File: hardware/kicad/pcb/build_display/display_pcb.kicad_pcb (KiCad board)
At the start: 2 copper layers, 85 x 65 mm, 43 parts, among them J1 Wurth_615008145521, J2 JST_S8B-PH-K-S, J3 ESP-Prog, J5 TERM, U1 R-78E3.3-0.5, U2 THVD1400DR, U3-LDO AP2112K-3.3, U4-MUX TPS2116DRLR

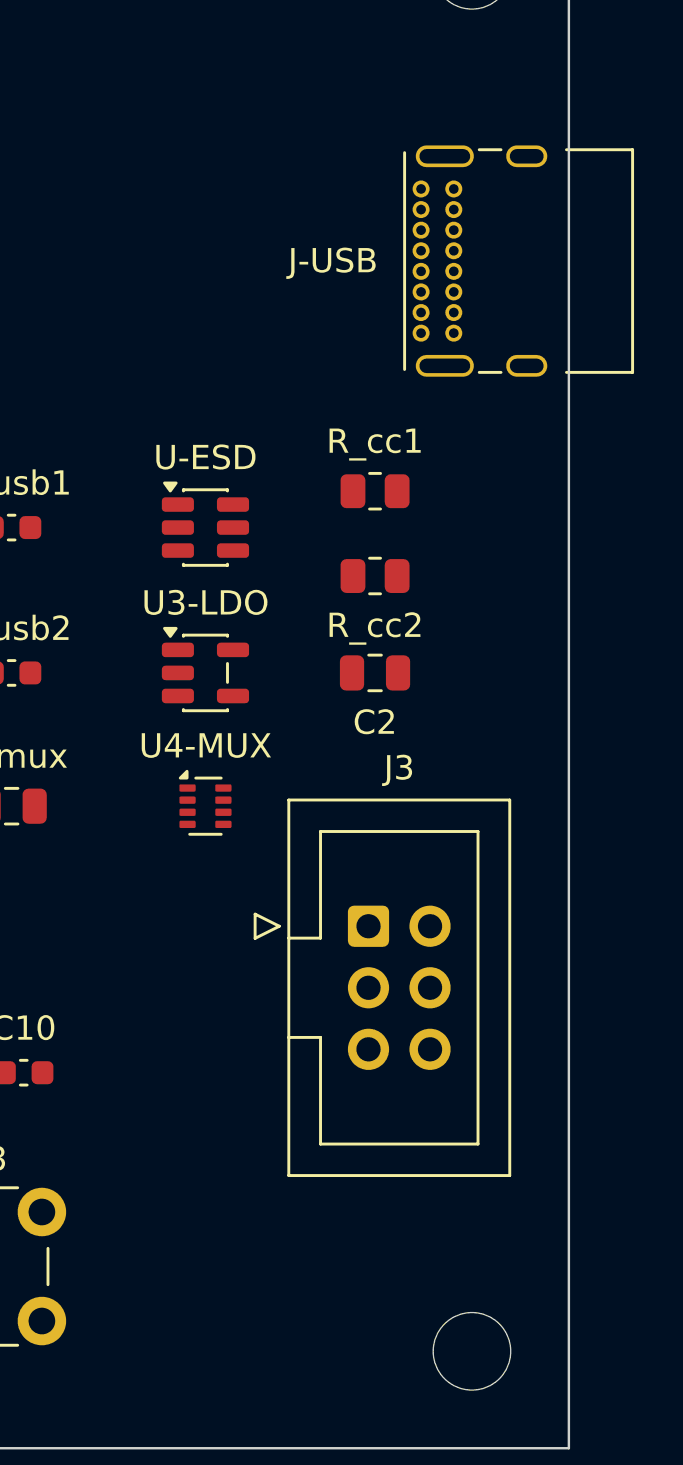
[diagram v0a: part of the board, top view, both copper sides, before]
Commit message: cp4: D40 vertical USB-C (resolves DR-35) + D41 no signing keys (resolves DR-34)
D40 - the edge-mount USB4085 could not be plugged inside the wall box (~5mm
past any board edge vs a plug needing 15-20mm; popping the faceplate exposes
the board FRONT, not its edges). User chose the vertical option: it opens +Z
and is reachable straight-on once the faceplate and e-paper module come away,
and is invisible when assembled.

Part is GCT USB4115-03-C (9.30mm) rather than the shorter USB4120 (6.5mm),
deliberately trading depth for footprint provenance: KiCad ships a footprint
for the 4115 citing GCT's official drawing and none for the 4120, and
hand-authoring a 0.5mm-pitch connector land pattern is the exact risk class
that produced DR-33 and the CP3 mating-face defect. Depth is affordable here;
a wrong land pattern is not.

Checked rather than assumed: pin table cross-read against the drawing (the
footprint's A1-A12/B1-B12/SH pads are a superset of our 16-pin symbol, so
every pin binds and the 8 SuperSpeed pads float); 30/30 pad tuples identical
to the library so the lib_footprint_mismatch is the same serialisation class
(evidence in iter1/jusb_pad_diff.txt); nothing overhangs a board edge any
more, so the E-edge whitelist is gone and silk_edge_clearance went 2 -> 0.
I ALSO CORRECTED MYSELF: I had claimed the taller part would force a longer
button plunger. It does not - with the 15mm plunger already locked the
protrusion is 2.3mm, inside the 2-3mm spec. The arithmetic is in D40.

Depth stack re-driven: J-USB 9.30mm displaces J3's 9.1mm, so gap ~9.7mm and
stack ~34.7mm against ~45mm usable. Battery board KEEPS USB4085 - it is not
in a wall box and its edge mount is correct there.

D41 - RPA sign-off stays name-based (git authorship), no signing keys. The
limit is stated in the gate's docstring rather than papered over, and the
threat model in REVIEWER_PATCH_POLICY.md explains why it is proportionate.

Stale-claim sweep after the change: requirements.md's exact-part list sti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
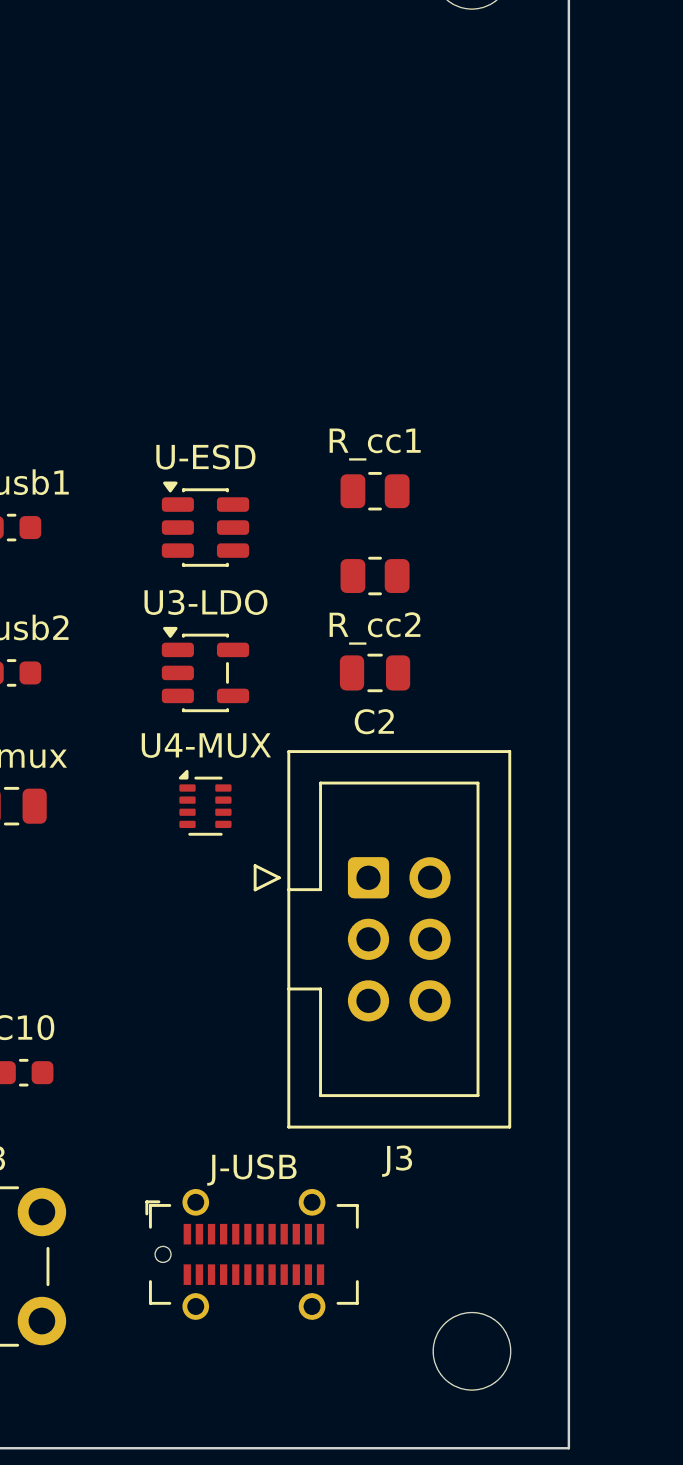
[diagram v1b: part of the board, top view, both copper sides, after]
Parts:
- removed the J-USB at (78.9, 19.0)
- added J-USB: USB4115-03-C, Connector_USB:USB_C_Receptacle_GCT_USB4115-03-C, F.Cu at (72.0, 57.0)
- moved J3 2.00 mm to (76.7, 41.5)

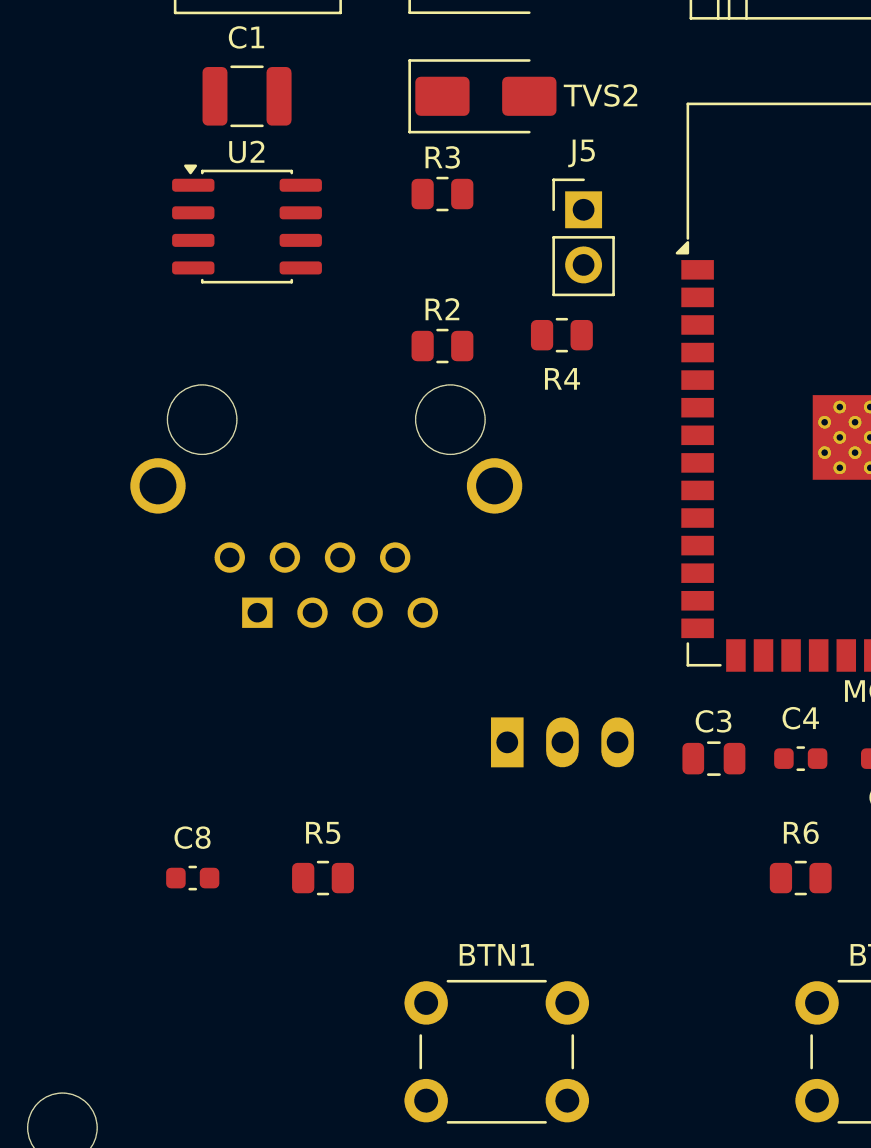
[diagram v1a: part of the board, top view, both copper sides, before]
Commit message: cp4 iter2: F01 back-side centre transform (4th site) + F02 wrong-order SKUs
F01 BLOCKER, confirmed and fixed at root. cc() in BOTH pcb builds still
negated local X while the writer and gates negate Y - the FOURTH site of a
transform I had "swept" twice. Reproduced the reviewer's numbers exactly: J1
requested (9.8,46.5) actually landed at (16.15,28.06), U1 (22,41) at
(26.97,45.50). The fix is not an axis edit: cc() now delegates to core._xf so
the project has exactly ONE back-side transform. A duplicated transform was
the bug; sharing it is the fix.

The J1 orientation assert was tautological, as reported - it compared two
symmetric X centroids, equal by construction. Replaced with a real probe: the
signal pads sit at one end of the footprint and the body extends away from
them, so the pads->courtyard-centre vector IS the opening direction. J1 is
now rot 90 on the back and that vector reads (-7.95,+0.00) = due west.

Re-placed for the three conflicts the corrected transform exposed (BTN1 into
J1 pads, J1 pads into R5, J1 courtyard into U1): J1 to (11,30), U1 to
(12,48), U2 to (25.5,33.5), R2 to (27,29). All gates and DRC clean; parts now
land exactly at their requested centres (error 0.00).

F02 IMPORTANT, confirmed by live POST /resolve: 455-1710-ND -> B8B-PH-K-S
(the REJECTED top-entry part) and 640-USB4085-GF-A -> USB4085-GF-A (the
retired edge part). Both cells would have ordered the wrong physical object.
Cause was incomplete propagation twice over - D39 changed the MPN text but
never re-resolved the order code, and D40 updated one distributor column and
not the other. Corrected both, plus the stale J-USB prose in
cp1_display_side.md and the J2 description that said "S8B" for both entries.

New persistent coverage: a ROW-SCOPED coherence check (a display BOM row must
not carry an order code that resolves to a different part than its own MPN).
Deliberately row-scoped, not a SUPERSEDED token, because the BATTERY J3
legitimately orders USB4085 through that exact Mo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
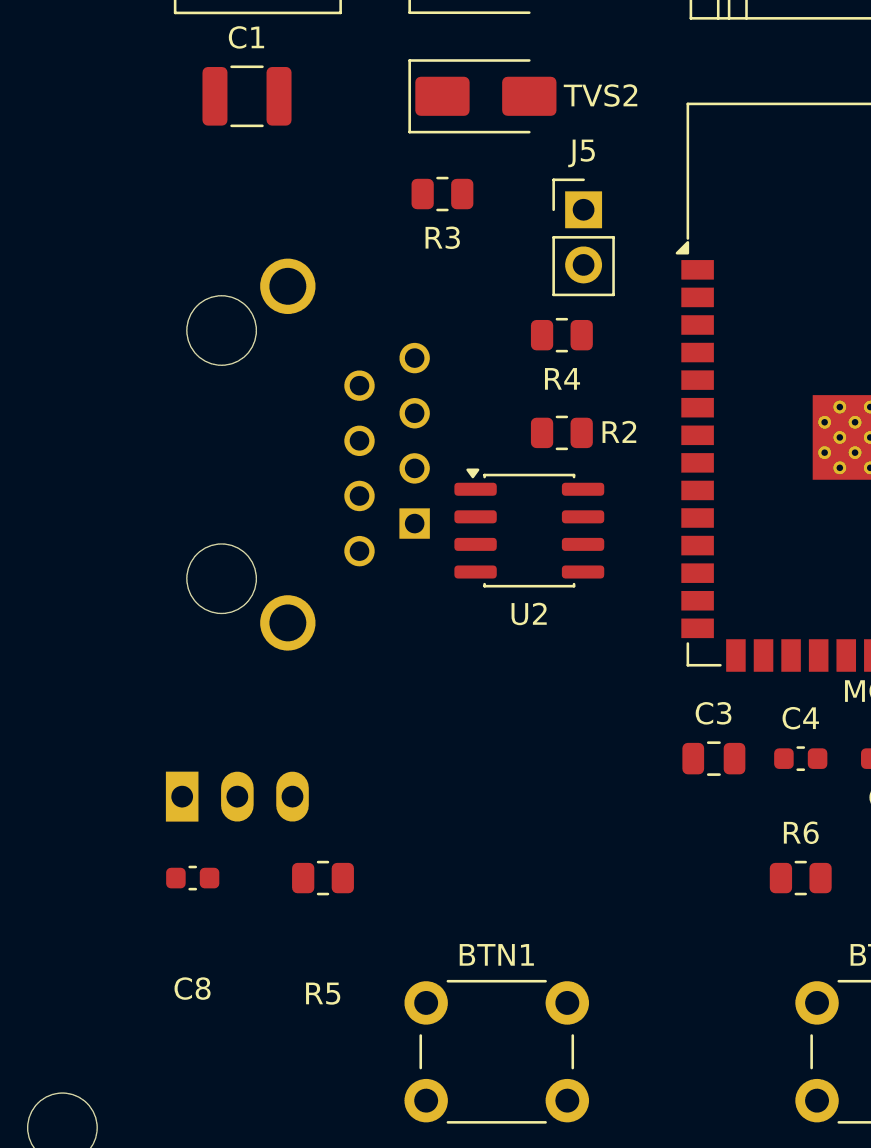
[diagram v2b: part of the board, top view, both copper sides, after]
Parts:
- moved U2 19.1 mm to (25.5, 33.5)
- moved U1 15.2 mm to (9.52, 45.8)
- moved J1 8.33 mm to (20.2, 33.2), turned to 90 degrees
- moved R2 6.80 mm to (27.0, 29.0)

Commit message: cp4 iter2: F03 envelope geometry + F04 retract the "exact match" claim
F03 - verified the reviewer's report: J1 references Wurth's own
WE_3DMODEL_DIR (unbound here), the stock USB footprint names a STEP absent
from this KiCad 10 install, and the buttons carry the H13 model against a
15mm selection. Took the reviewer's second option - committed dimensioned
envelope geometry - as more deterministic than hand-authoring 3D solids.
Every height-critical part now carries a Cmts.User envelope rectangle plus a
height label sourced to its datasheet, exported as doc_envelopes.svg/PDF:
J1 13.6 (B), U1 11.0 (B), J-USB 9.30 (F), J3 9.10 (F), J2 7.60 (F),
BTN1-3 15.0 (F).

That plot earned its keep immediately: it showed the board still carrying
"Antenna KEEP-OUT ZONE" on Cmts.User from the stock ESP32 footprint -
asserting in the board's own documentation exactly the constraint D26 retired
and D39 built a variant to drop. Removed from the variant (the factual
"Antenna" label stays); provenance recorded in the footprints README. That is
a second, independent way the keepout was still live after I claimed to have
implemented D26.

F04 - the worst of the four, and entirely mine. The datasheet specifies 4 x
1.0mm drills; the footprint uses 1.1mm. My own console output printed
"drill 1.1" on the same screen where I wrote "exact match" - a verification
adjective contradicted by evidence in front of me, which is the precise
failure my own skills tell me to hunt. Every such claim replaced with the
stated 1.0->1.1 deviation and an acceptance argument: centres match exactly,
the 0.7 +/-0.1mm terminal leaves >=0.3mm diametral clearance in a 1.1mm hole,
and the 2.0mm pad keeps a 0.45mm annular ring - far above the 0.13mm fab
floor. Sane substitution, NOT identity evidence.

Packet 9.1 written with per-finding root-cause accounting; hashes refreshed
(board 6232b530ee70). Battery board byte-identical (448d59a276df).

Co-Authored-By: Claude Fable 5 <noreply@anthropic.com>
Claude-Session: https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
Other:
- board text added: "BTN1 h=15.0mm (F)"
- board text added: "BTN2 h=15.0mm (F)"
- board text added: "BTN3 h=15.0mm (F)"
- board text added: "J-USB h=9.3mm (F)"
- board text added: "J1 h=13.6mm (B)"
- board text added: "J2 h=7.6mm (F)"
- board text added: "J3 h=9.1mm (F)"
- board text added: "U1 h=11.0mm (B)"
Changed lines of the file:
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@@
       (effects (font (size 1 1) (thickness 0.15)))
-    )
-    (fp_text user "KEEP-OUT ZONE" (at 0 -18.92 0) (layer "Cmts.User")
-      (effects (font (size 2 2) (thickness 0.15)))
     )
     (fp_text user "${REFERENCE}" (at 0 -0.6 0) (layer "F.Fab")
@@
   (gr_line (start 85.0 65.0) (end 0 65.0) (layer "Edge.Cuts") (width 0.1))
   (gr_line (start 0 65.0) (end 0 0) (layer "Edge.Cuts") (width 0.1))
+  (gr_rect (start 21.0 54.5) (end 27.0 60.5) (layer "Cmts.User") (width 0.05) (fill none))
+  (gr_text "BTN1 h=15.0mm (F)" (at 24.0 53.6 0) (layer "Cmts.User")
+    (effects (font (size 0.7 0.7) (thickness 0.12)))
+  )
+  (gr_rect (start 39.0 54.5) (end 45.0 60.5) (layer "Cmts.User") (width 0.05) (fill none))
+  (gr_text "BTN2 h=15.0mm (F)" (at 42.0 53.6 0) (layer "Cmts.User")
+    (effects (font (size 0.7 0.7) (thickness 0.12)))
+  )
+  (gr_rect (start 57.0 54.5) (end 63.0 60.5) (layer "Cmts.User") (width 0.05) (fill none))
+  (gr_text "BTN3 h=15.0mm (F)" (at 60.0 53.6 0) (layer "Cmts.User")
+    (effects (font (size 0.7 0.7) (thickness 0.12)))
+  )
+  (gr_rect (start 67.53 54.85) (end 76.47 59.15) (layer "Cmts.User") (width 0.05) (fill none))
+  (gr_text "J-USB h=9.3mm (F)" (at 72.0 53.95 0) (layer "Cmts.User")
+    (effects (font (size 0.7 0.7) (thickness 0.12)))
+  )
+  (gr_rect (start 0.43 22.1) (end 21.57 37.9) (layer "Cmts.User") (width 0.05) (fill none))
+  (gr_text "J1 h=13.6mm (B)" (at 11.0 21.2 0) (layer "Cmts.User")
+    (effects (font (size 0.7 0.7) (thickness 0.12)))
+  )
+  (gr_rect (start 33.05 2.2) (end 50.95 9.8) (layer "Cmts.User") (width 0.05) (fill none))
+  (gr_text "J2 h=7.6mm (F)" (at 42.0 1.3 0) (layer "Cmts.User")
+    (effects (font (size 0.7 0.7) (thickness 0.12)))
+  )
+  (gr_rect (start 73.55 36.355) (end 82.45 51.635) (layer "Cmts.User") (width 0.05) (fill none))
+  (gr_text "J3 h=9.1mm (F)" (at 78.0 35.455 0) (layer "Cmts.User")
+    (effects (font (size 0.7 0.7) (thickness 0.12)))
+  )
+  (gr_rect (start 6.205 43.75) (end 17.805 52.25) (layer "Cmts.User") (width 0.05) (fill none))
+  (gr_text "U1 h=11.0mm (B)" (at 12.005 42.85 0) (layer "Cmts.User")
+    (effects (font (size 0.7 0.7) (thickness 0.12)))
+  )
 )
